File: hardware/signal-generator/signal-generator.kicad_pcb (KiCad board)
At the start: 4 copper layers, 151 parts, among them J1 AVR-ISP-6, J10 Output_Conn, J11 SD_Card_Conn, J12 TP_Conn, J13 LCD_Conn, J2 AVR_SPI, J3 PORT_G, J4 PORT_F, J5 PORT_E, J6 PORT_A, J7 PORT_C, J8 AREF, J9 Power_Supply_Rails, Q1 MMBF5485, Q10 AP2310GN, Q11 AP2310GN, Q12 AP2310GN, Q2 MMBF5485, Q3 MMBF5485, Q4 AP2310GN, Q5 AP2310GN, Q6 AP2310GN, Q7 AP2310GN, Q8 AP2310GN, Q9 AP2310GN, SW1 RESET_BUTTON, U1 74HC04, U10 MCP23017-E/SO, U11 AD9764AR, U12 TS4061AICT-1.25, U13 74HC4040, U14 74HC4040, U15 MCP4551-103E/MS, U16 AD8021ARZ, U17 AD8021ARZ, U18 MCP4716, U19 AD8021ARZ, U2 74HC08, U20 MIC6211, U21 AZ431AN-A, U22 AD8021ARZ, U3 74HC08, U4 74HC30, U5 ATmega2561-16AU, U6 ADP7142AUJZ-5.0, U7 TC1017-3.3VCTTR, U8 DS1085Z-10+, U9 CY7C1021D-10ZSXI, Y1 16MHz

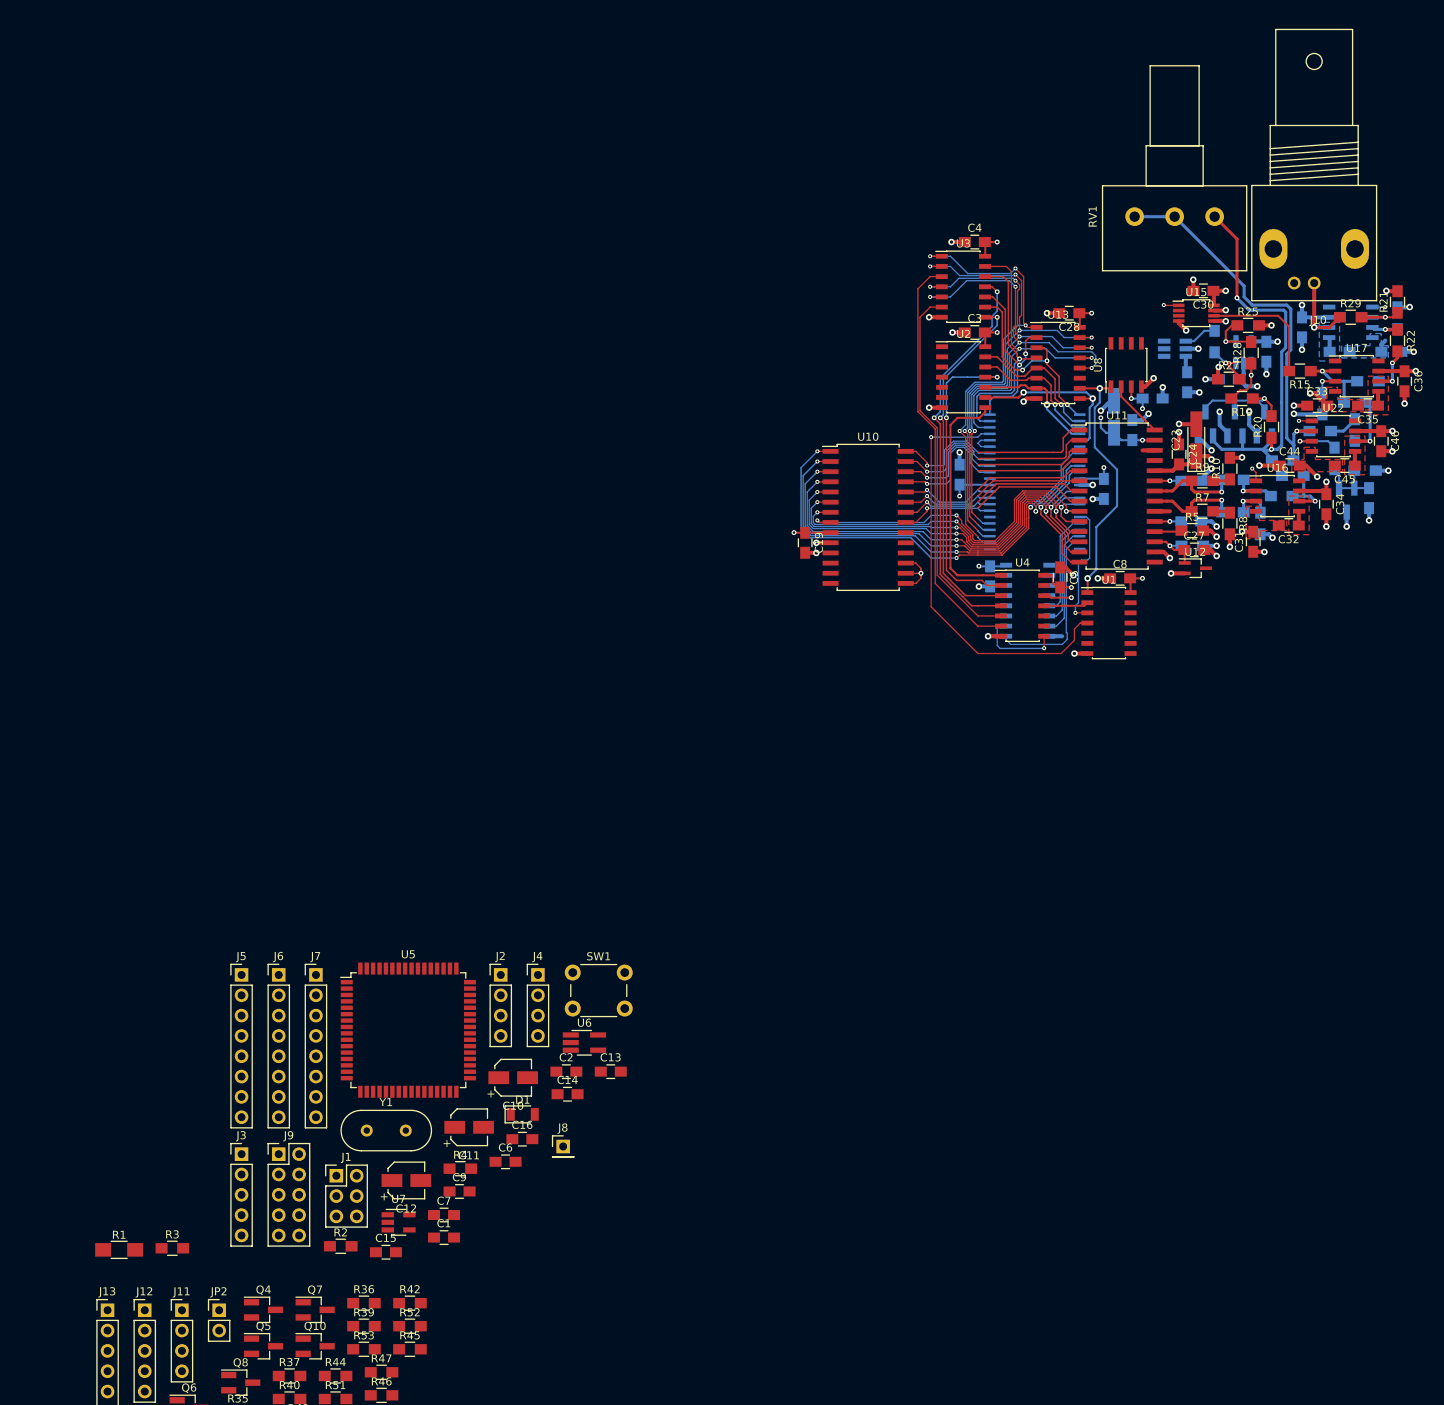
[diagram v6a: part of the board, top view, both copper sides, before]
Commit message: [Signal Generator] Layout microcontroller and its peripheral components
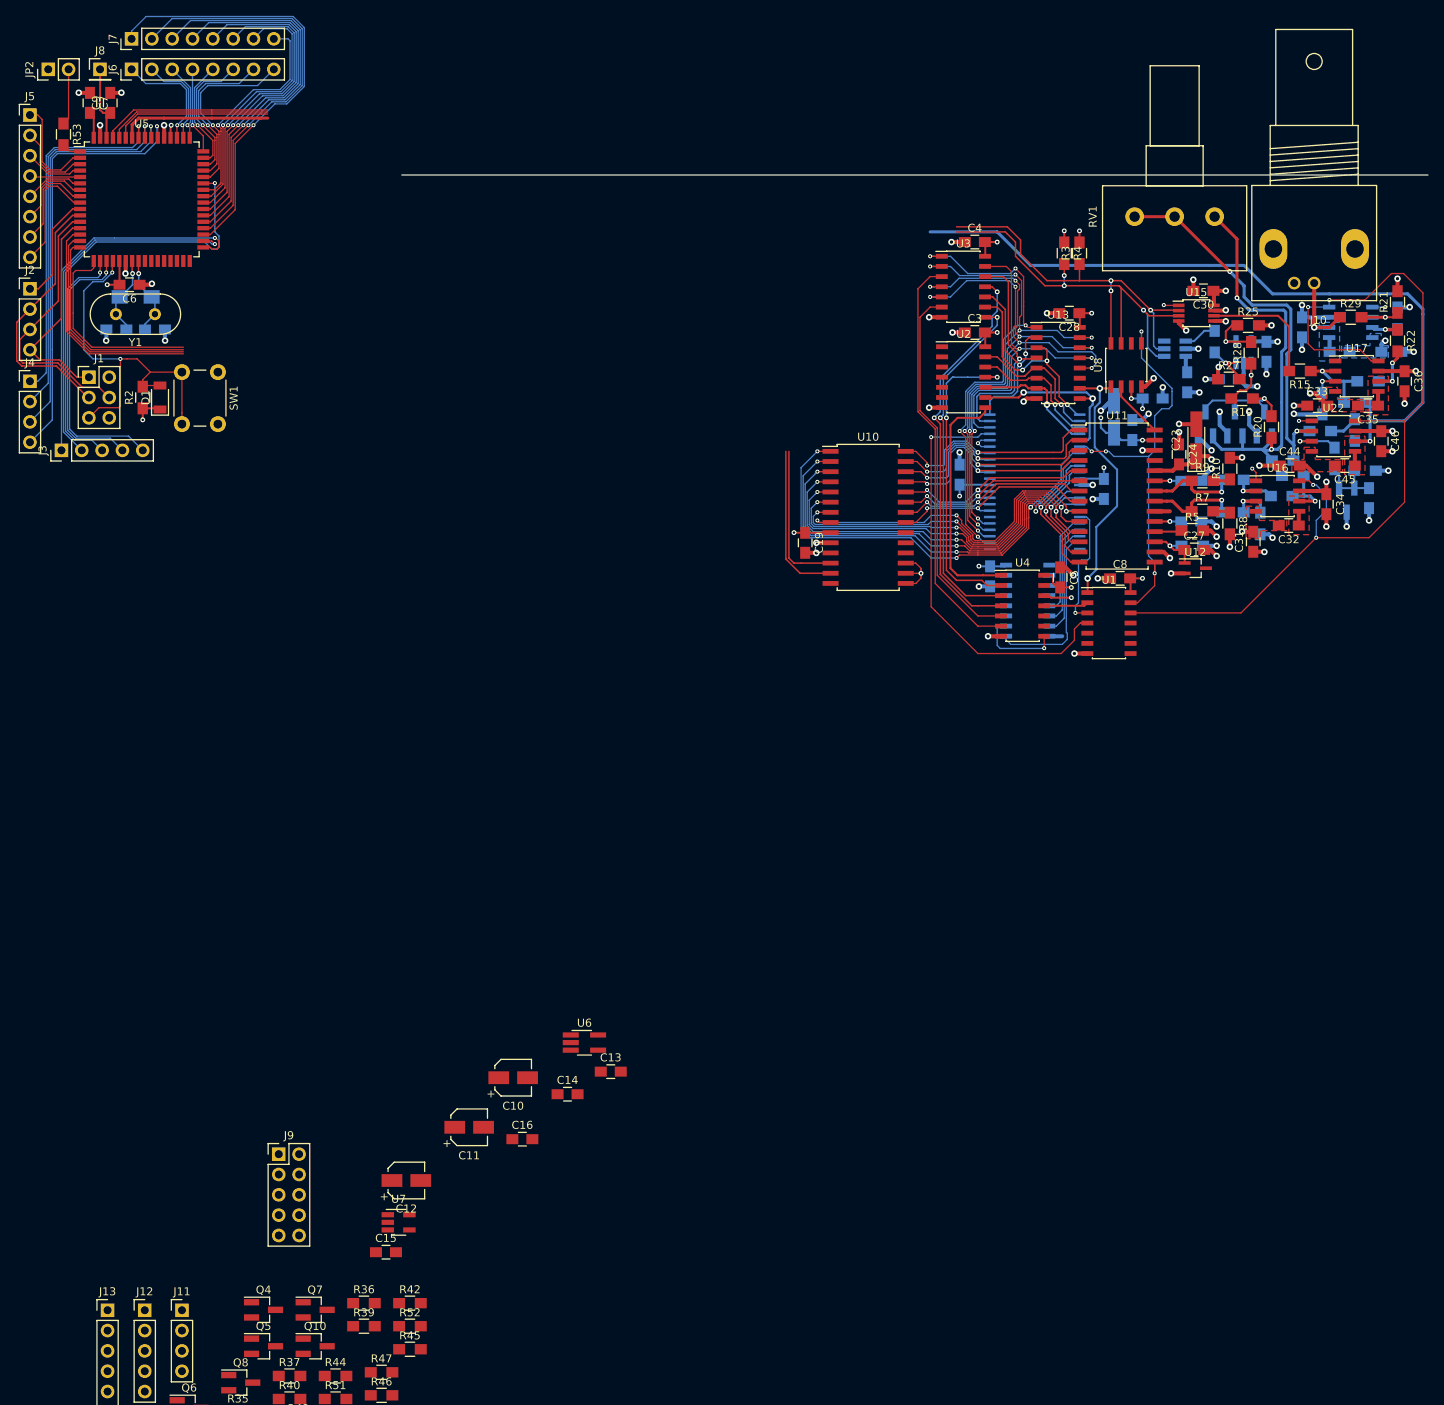
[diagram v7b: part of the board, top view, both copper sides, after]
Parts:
- C1, C2, R1: moved to B.Cu
- moved R3 168.3 mm to (152.8, 42.3), turned to 90 degrees
- moved JP2 156.6 mm to (23.9, 19.3), turned to 90 degrees
- moved R53 156.4 mm to (25.8, 27.4), turned to 270 degrees
- moved J8 146.6 mm to (30.4, 19.3)
- moved C7 145.9 mm to (29.1, 23.5), turned to 270 degrees
- moved C9 142.9 mm to (31.6, 23.5), turned to 90 degrees
- moved R4 137.1 mm to (150.9, 42.3), turned to 270 degrees
- moved C6 119.3 mm to (34.0, 46.2), turned to 180 degrees
- moved J7 119.3 mm to (34.3, 15.5), turned to 90 degrees
- moved R1 119.1 mm to (34.8, 47.8)
- moved C1 119.1 mm to (37.2, 51.8)
- moved J6 114.7 mm to (34.3, 19.3), turned to 90 degrees
- moved J5 110.7 mm to (21.6, 25.0)
- moved U5 109.1 mm to (35.6, 35.6)
- moved R2 108.9 mm to (35.7, 60.3), turned to 90 degrees
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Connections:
- J13 pad 8: AGND -> /TFT LCD Module Interface Block/LCD_BL
- JP2 pad 2: AGND -> /TFT LCD Module Interface Block/LCD_BL
- R53 pad 1: AGND -> /TFT LCD Module Interface Block/LCD_BL
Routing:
- net /Output Circuitry/~DISABLE: track 0.00 -> 115.1 mm, vias 0 -> 4
- net /OCAL: track 8.85 -> 112.6 mm
- net /PWRDWN: track 0.00 -> 72.6 mm, vias 0 -> 4
- net /SDA: track 0.00 -> 70.4 mm, vias 0 -> 3
- net /SCL: track 0.00 -> 68.0 mm, vias 0 -> 3
- net Net-(J7-Pad1): track 0.00 -> 56.4 mm, vias 0 -> 1
- net Net-(J3-Pad3): track 0.00 -> 56.3 mm, vias 0 -> 1
- net Net-(J4-Pad4): track 0.00 -> 54.0 mm, vias 0 -> 1
- net Net-(J7-Pad2): track 0.00 -> 52.0 mm, vias 0 -> 1
- net Net-(J4-Pad3): track 0.00 -> 50.9 mm, vias 0 -> 1
- net Net-(J7-Pad3): track 0.00 -> 48.2 mm, vias 0 -> 1
- net /~RESET: track 0.00 -> 48.1 mm, vias 0 -> 2
- net Net-(J4-Pad2): track 0.00 -> 47.8 mm, vias 0 -> 1
- net Net-(J3-Pad1): track 0.00 -> 46.9 mm, vias 0 -> 1
- net Net-(J3-Pad2): track 0.00 -> 45.7 mm, vias 0 -> 1
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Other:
- net class SPI added: clearance 0.127, trace_width 0.1905, via_dia 0.6096, via_drill 0.3048

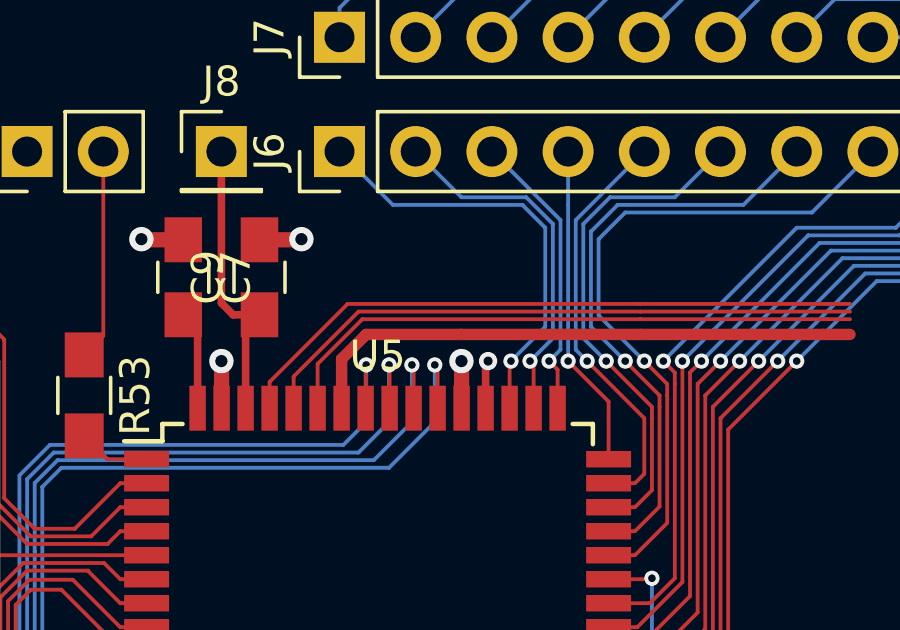
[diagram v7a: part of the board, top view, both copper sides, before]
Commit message: [Signal Generator] Add an additional bypass capacitor to MCU
The ATMega2561's package has additional power supply pins (for +VCC and
GND). They are hidden in the schematic symbol in KiCad. Nevertheless,
an additional bypass capacitor which is annotated as 'C47' has been
included in the schematic and PCB.
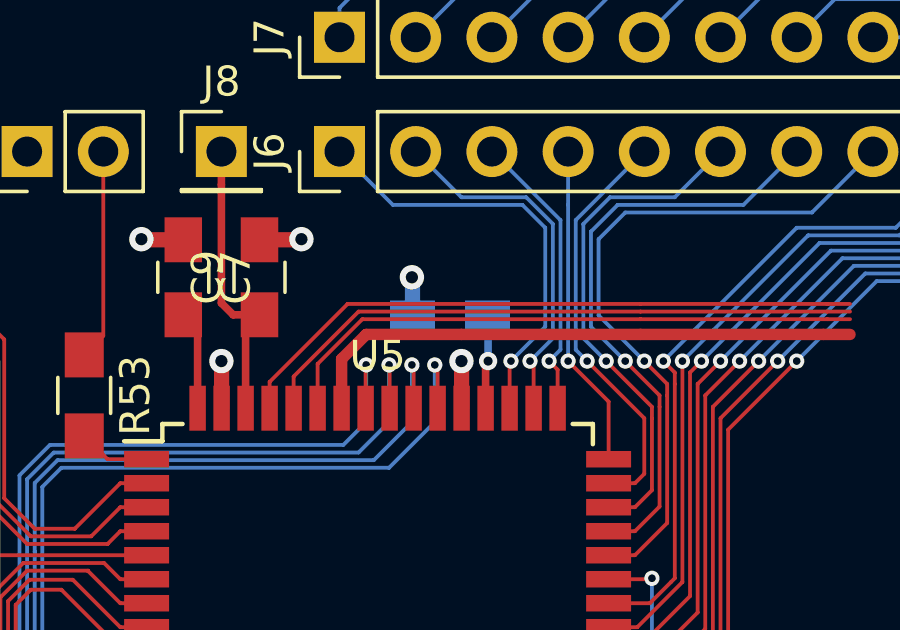
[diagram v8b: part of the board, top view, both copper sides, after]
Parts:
- added C47: 100nF, Capacitors_SMD:C_0805_HandSoldering, B.Cu at (38.0, 24.9)
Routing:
- net +5VD: track 68.0 -> 69.4 mm
- net AGND: track 127.5 -> 128.9 mm, vias 67 -> 68
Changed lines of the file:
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@@
     (thickness 1.6)
     (drawings 1)
-    (tracks 1931)
+    (tracks 1936)
     (zones 0)
-    (modules 151)
+    (modules 152)
     (nets 184)
   )
@@
   (title_block
     (title "Digital Function Generator v2")
-    (date 2020-01-02)
+    (date 2020-01-03)
     (rev 1)
     (company "Petar Nikolov")
@@
     )
   )
+  (module Capacitors_SMD:C_0805_HandSoldering (layer B.Cu)
+    (at 37.973 24.892 180)
+    (descr "Capacitor SMD 0805, hand soldering")
+    (tags "capacitor 0805")
+    (attr smd)
+    (fp_text reference C47 (at 0 1.75) (layer B.SilkS)
+      (effects (font (size 1 1) (thickness 0.15)) (justify mirror))
+    )
+    (fp_text value 100nF (at 0 -1.75) (layer B.Fab)
+      (effects (font (size 1 1) (thickness 0.15)) (justify mirror))
+    )
+    (fp_line (start 2.25 -0.87) (end -2.25 -0.87) (layer B.CrtYd) (width 0.05))
+    (fp_line (start 2.25 -0.87) (end 2.25 0.88) (layer B.CrtYd) (width 0.05))
+    (fp_line (start -2.25 0.88) (end -2.25 -0.87) (layer B.CrtYd) (width 0.05))
+    (fp_line (start -2.25 0.88) (end 2.25 0.88) (layer B.CrtYd) (width 0.05))
+    (fp_line (start -0.5 -0.85) (end 0.5 -0.85) (layer B.SilkS) (width 0.12))
+    (fp_line (start 0.5 0.85) (end -0.5 0.85) (layer B.SilkS) (width 0.12))
+    (fp_line (start -1 0.62) (end 1 0.62) (layer B.Fab) (width 0.1))
+    (fp_line (start 1 0.62) (end 1 -0.62) (layer B.Fab) (width 0.1))
+    (fp_line (start 1 -0.62) (end -1 -0.62) (layer B.Fab) (width 0.1))
+    (fp_line (start -1 -0.62) (end -1 0.62) (layer B.Fab) (width 0.1))
+    (fp_text user %R (at 0 1.75) (layer B.Fab)
+      (effects (font (size 1 1) (thickness 0.15)) (justify mirror))
+    )
+    (pad 2 smd rect (at 1.25 0 180) (size 1.5 1.25) (layers B.Cu B.Paste B.Mask)
+      (net 1 AGND))
+    (pad 1 smd rect (at -1.25 0 180) (size 1.5 1.25) (layers B.Cu B.Paste B.Mask)
+      (net 4 +5VD))
+    (model Capacitors_SMD.3dshapes/C_0805.wrl
+      (at (xyz 0 0 0))
+      (scale (xyz 1 1 1))
+      (rotate (xyz 0 0 0))
+    )
+  )
   (gr_line (start 196.342 32.512) (end 68.072 32.512) (layer Edge.Cuts) (width 0.05))
   (segment (start 165.929 82.311) (end 164.226 82.311) (width 0.508) (layer F.Cu) (net 1))
@@
   (segment (start 31.623 22.245) (end 33 22.245) (width 0.508) (layer F.Cu) (net 1))
   (segment (start 33 22.245) (end 33.02 22.225) (width 0.508) (layer F.Cu) (net 1))
+  (via (at 36.703 23.495) (size 0.8128) (drill 0.4064) (layers F.Cu B.Cu) (net 1))
+  (segment (start 36.723 24.892) (end 36.723 23.515) (width 0.508) (layer B.Cu) (net 1))
+  (segment (start 36.723 23.515) (end 36.703 23.495) (width 0.508) (layer B.Cu) (net 1))
   (segment (start 36.798 47.244) (end 36.703 47.244) (width 0.1905) (layer B.Cu) (net 2))
   (segment (start 35.961 51.161) (end 35.961 51.816) (width 0.1905) (layer B.Cu) (net 2))
@@
   (segment (start 32.786 43.286) (end 32.76 43.26) (width 0.254) (layer F.Cu) (net 4))
   (segment (start 32.786 46.228) (end 32.786 43.286) (width 0.254) (layer F.Cu) (net 4))
-  (segment (start 39.16 27.86) (end 39.16 26.372) (width 0.254) (layer F.Cu) (net 4))
-  (via (at 39.243 26.289) (size 0.6096) (drill 0.3048) (layers F.Cu B.Cu) (net 4))
-  (segment (start 39.16 26.372) (end 39.243 26.289) (width 0.254) (layer F.Cu) (net 4))
   (segment (start 29.56 25.222) (end 29.083 24.745) (width 0.254) (layer F.Cu) (net 4))
   (segment (start 29.56 27.86) (end 29.56 25.222) (width 0.254) (layer F.Cu) (net 4))
@@
   (via (at 31.242 46.228) (size 0.6096) (drill 0.3048) (layers F.Cu B.Cu) (net 4))
   (segment (start 32.786 46.228) (end 31.242 46.228) (width 0.254) (layer F.Cu) (net 4))
+  (via (at 39.243 26.289) (size 0.6096) (drill 0.3048) (layers F.Cu B.Cu) (net 4))
+  (segment (start 39.16 27.86) (end 39.16 26.372) (width 0.254) (layer F.Cu) (net 4))
+  (segment (start 39.16 26.372) (end 39.243 26.289) (width 0.254) (layer F.Cu) (net 4))
+  (segment (start 39.243 24.912) (end 39.223 24.892) (width 0.254) (layer B.Cu) (net 4))
+  (segment (start 39.243 26.289) (end 39.243 24.912) (width 0.254) (layer B.Cu) (net 4))
   (segment (start 30.353 20.408) (end 30.353 19.304) (width 0.254) (layer F.Cu) (net 5))
   (segment (start 30.353 24.354) (end 30.353 20.408) (width 0.254) (layer F.Cu) (net 5))
